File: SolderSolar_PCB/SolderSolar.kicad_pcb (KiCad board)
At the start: 2 copper layers, 50 x 37.5 mm, 13 parts, among them P1 SOLAR_V, P2 LOGO1, P3 LOGO2, P5 LOGO3, SW1 RED, SW2 WHITE

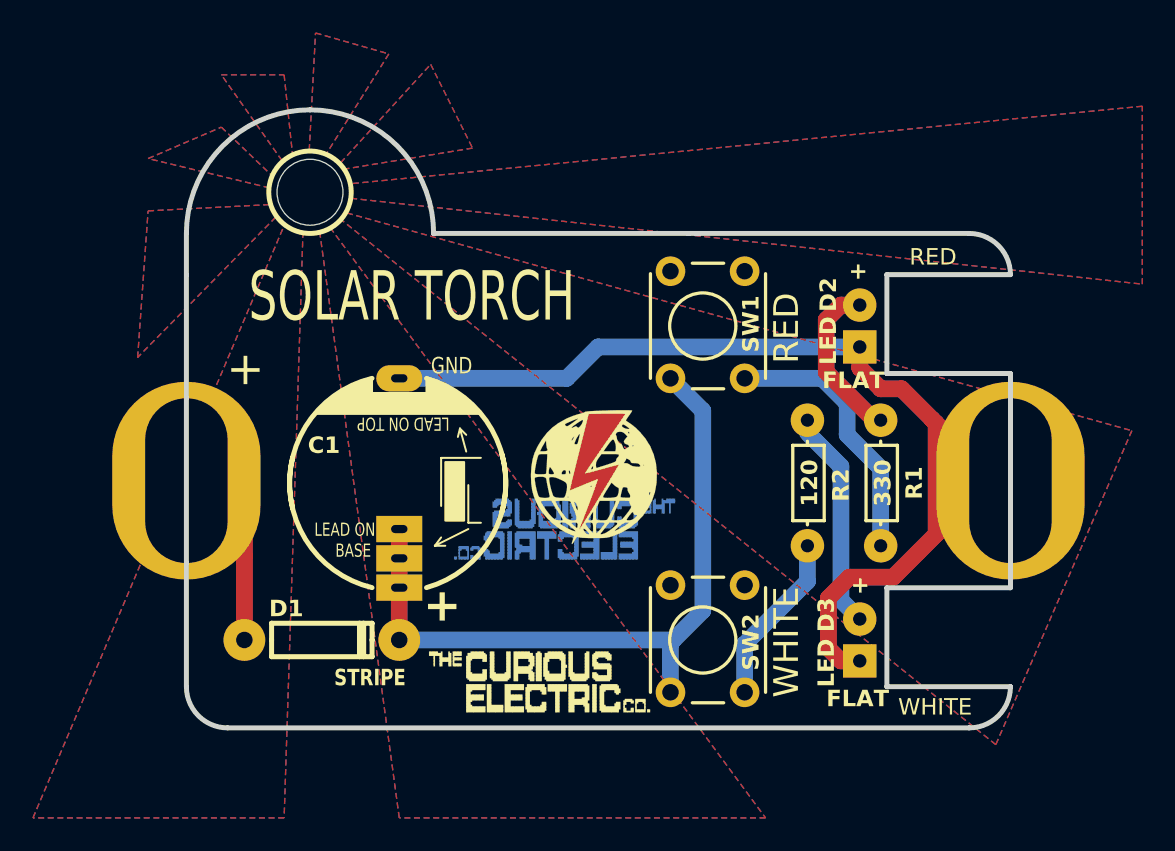
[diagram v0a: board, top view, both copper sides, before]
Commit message: changed hole size for production
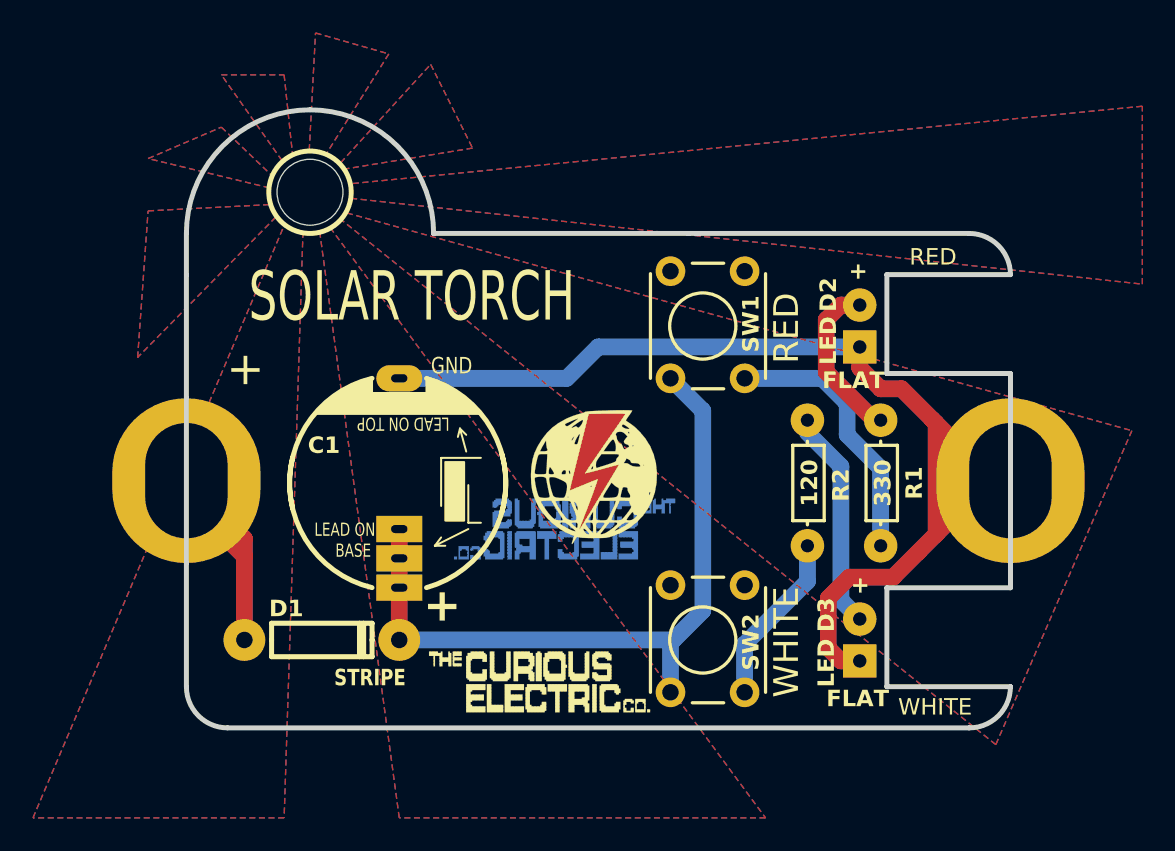
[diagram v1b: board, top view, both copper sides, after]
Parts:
- SC1: footprint REInnovationFootprint:PV_50x30mm_NoOutline -> REInnovationFootprint:PV_50x30mm_NoOutline_v2
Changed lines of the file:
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@@
 		)
 	)
-	(footprint "REInnovationFootprint:PV_50x30mm_NoOutline"
+	(footprint "REInnovationFootprint:PV_50x30mm_NoOutline_v2"
 		(layer "F.Cu")
 		(at 154.559 73.279 90)
@@
 			)
 		)
-		(property "Footprint" "REInnovationFootprint:PV_50x30mm_NoOutline"
+		(property "Footprint" "REInnovationFootprint:PV_50x30mm_NoOutline_v2"
 			(at 0 0 90)
 			(layer "F.Fab")
@@
 		(pad "1" thru_hole oval
 			(at 15 -50 90)
-			(size 12 9)
-			(drill oval 10 5)
+			(size 10 9)
+			(drill oval 7 5)
 			(layers "*.Cu" "*.Mask")
 			(remove_unused_layers no)
@@
 		(pad "2" thru_hole oval
 			(at 15 0 90)
-			(size 12 9)
-			(drill oval 10 5)
+			(size 10 9)
+			(drill oval 7 5)
 			(layers "*.Cu" "*.Mask")
 			(remove_unused_layers no)
